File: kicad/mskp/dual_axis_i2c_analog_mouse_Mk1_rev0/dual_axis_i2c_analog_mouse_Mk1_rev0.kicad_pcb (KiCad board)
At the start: 2 copper layers, 17 parts, among them J1 I2C_controller_JST, J2 I2C_controller_pads, J3 mouse_input_pads, J4 mouse_input_JST, J5 Alert_pad, U1 AMS1117-3.3, U2 ADS1115IDGS

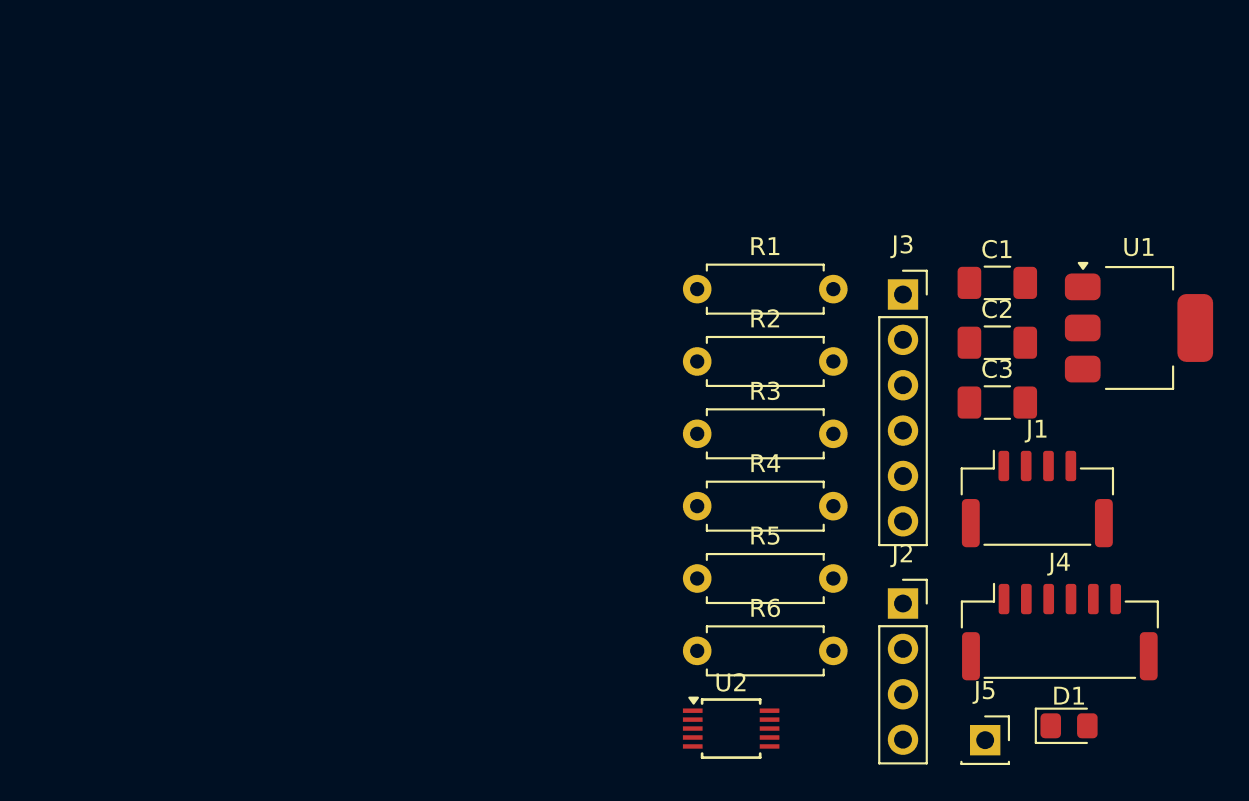
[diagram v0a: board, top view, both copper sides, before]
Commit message: Begins rough PCB part grouping for all control board revisions
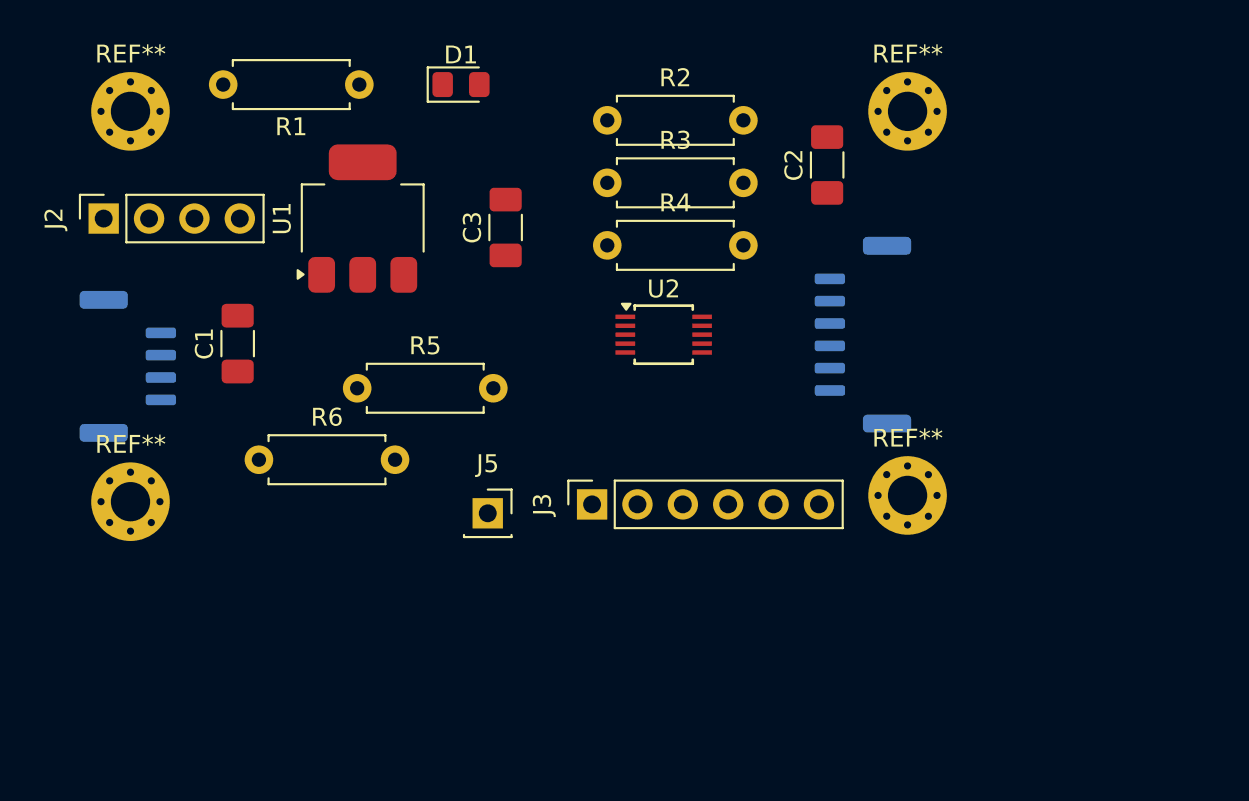
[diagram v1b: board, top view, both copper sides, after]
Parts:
- added REF**: MountingHole_2.2mm_M2_Pad_Via, MountingHole:MountingHole_2.2mm_M2_Pad_Via, F.Cu at (149.5, 69.5)
- added REF**: MountingHole_2.2mm_M2_Pad_Via, MountingHole:MountingHole_2.2mm_M2_Pad_Via, F.Cu at (149.5, 91.0)
- added REF**: MountingHole_2.2mm_M2_Pad_Via, MountingHole:MountingHole_2.2mm_M2_Pad_Via, F.Cu at (106.0, 69.5)
- added REF**: MountingHole_2.2mm_M2_Pad_Via, MountingHole:MountingHole_2.2mm_M2_Pad_Via, F.Cu at (106.0, 91.3)
- J1, J4: moved to B.Cu
- moved J1 51.5 mm to (105.8, 83.8), turned to 90 degrees
- moved J2 49.7 mm to (104.5, 75.5), turned to 90 degrees
- moved D1 49.5 mm to (124.5, 68.0)
- moved U1 43.9 mm to (119.0, 75.5), turned to 90 degrees
- moved C1 42.7 mm to (112.0, 82.5), turned to 90 degrees
- moved J5 30.6 mm to (126.0, 92.0)
- moved C3 29.2 mm to (127.0, 76.0), turned to 90 degrees
- moved R6 26.8 mm to (113.2, 89.0)
- moved U2 22.4 mm to (135.8, 82.0)
- moved R1 22.1 mm to (118.8, 68.0), turned to 180 degrees
- moved R5 21.8 mm to (118.7, 85.0)
- moved J3 21.0 mm to (131.8, 91.5), turned to 90 degrees
- moved J4 20.0 mm to (147.0, 82.0), turned to -90 degrees
- moved R4 15.4 mm to (132.7, 77.0)
- moved R3 14.9 mm to (132.7, 73.5)
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
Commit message: Continues work with rough PCB outlines
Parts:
- moved C2 16.9 mm to (138.4, 88.0), turned to 0 degrees
- moved J3 5.40 mm to (126.4, 91.4)
- moved REF** 5.15 mm to (144.8, 71.6)
- moved REF** 4.94 mm to (144.6, 90.4)
- moved R6 4.72 mm to (114.2, 84.4), turned to -90 degrees
- moved REF** 4.02 mm to (109.8, 70.8)
- moved J5 3.85 mm to (122.2, 91.4)
- moved R1 3.67 mm to (122.0, 69.8)
- moved U2 3.50 mm to (132.4, 82.6)
- moved C1 3.18 mm to (114.2, 80.2)
- moved REF** 2.51 mm to (108.4, 90.6)
- moved U1 2.48 mm to (120.6, 77.4)
- moved D1 2.33 mm to (126.2, 69.6), turned to 180 degrees
- moved C3 2.25 mm to (126.8, 78.2)
- moved J1 2.18 mm to (107.8, 82.8)
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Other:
- board outline added: 43.6 x 26.4 mm

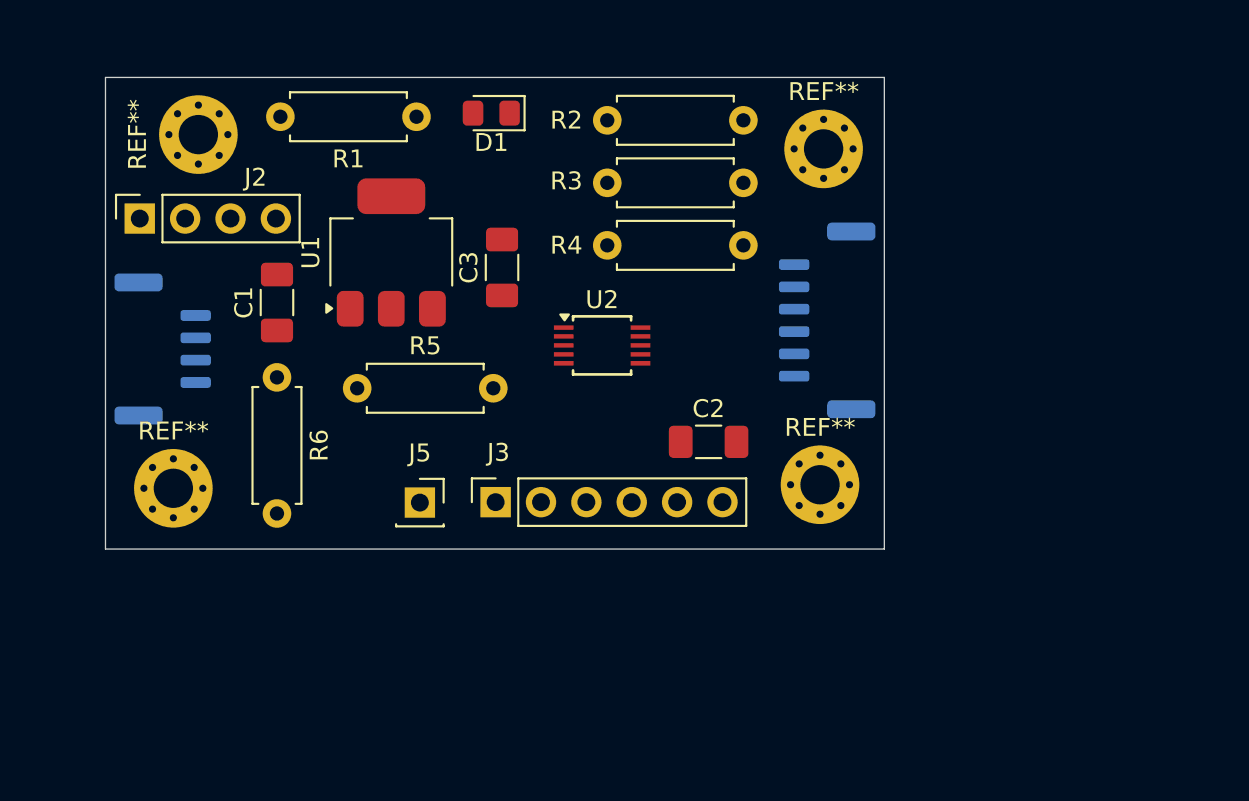
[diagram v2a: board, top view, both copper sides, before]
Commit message: Refines usb and mouse control boards with outline and GND
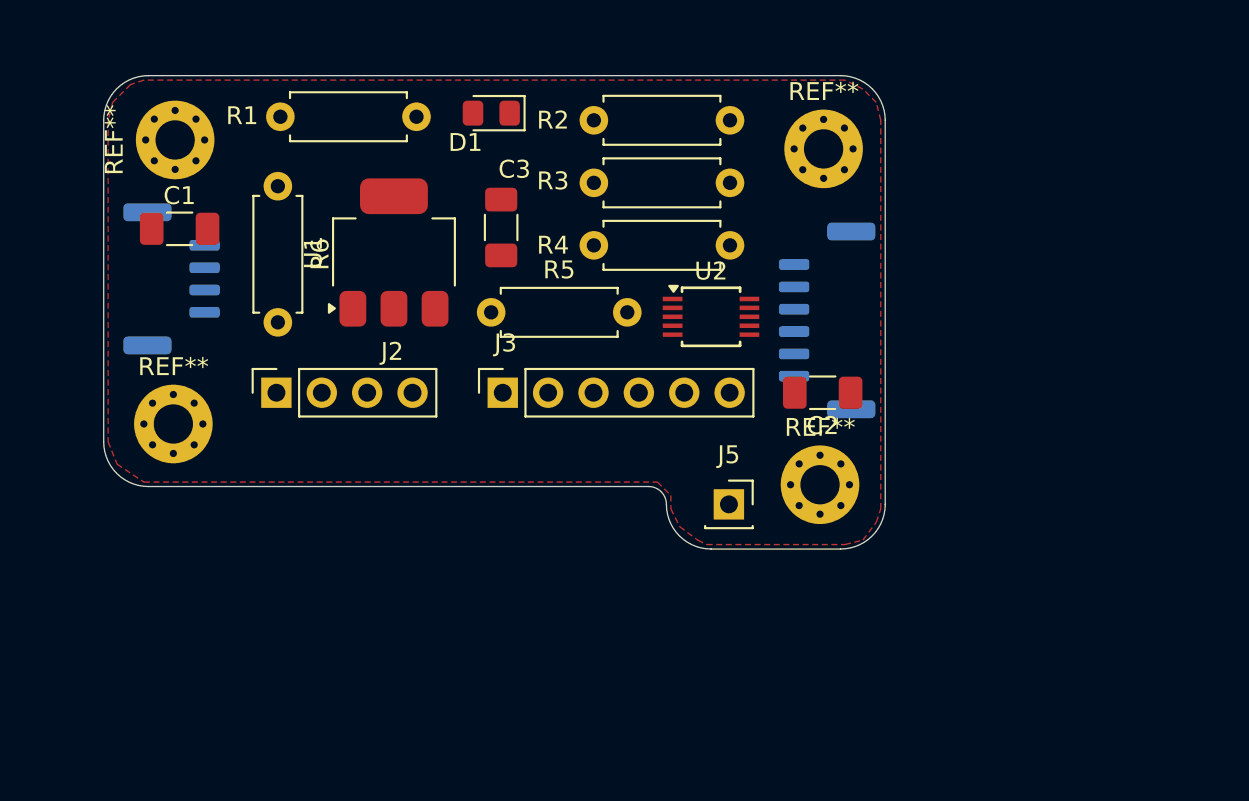
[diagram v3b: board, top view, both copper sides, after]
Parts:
- moved J5 17.3 mm to (139.5, 91.5)
- moved J2 12.4 mm to (114.2, 85.2)
- moved R6 10.7 mm to (114.2, 73.7)
- moved R5 8.62 mm to (126.2, 80.8)
- moved C2 6.95 mm to (144.8, 85.2), turned to 180 degrees
- moved C1 6.84 mm to (108.8, 76.1), turned to 0 degrees
- moved U2 6.31 mm to (138.5, 81.0)
- moved J3 6.14 mm to (126.8, 85.2)
- moved J1 3.96 mm to (108.3, 78.9)
- moved REF** 3.60 mm to (108.4, 87.0)
- moved C3 2.24 mm to (126.8, 76.0)
- moved REF** 1.33 mm to (108.5, 71.1)
- moved R2 0.75 mm to (131.9, 70.0)
- moved R3 0.75 mm to (131.9, 73.5)
- moved R4 0.75 mm to (131.9, 77.0)
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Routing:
- added copper zone on F.Cu, net GND
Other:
- board size 43.6 x 26.4 mm -> 43.8 x 26.5 mm

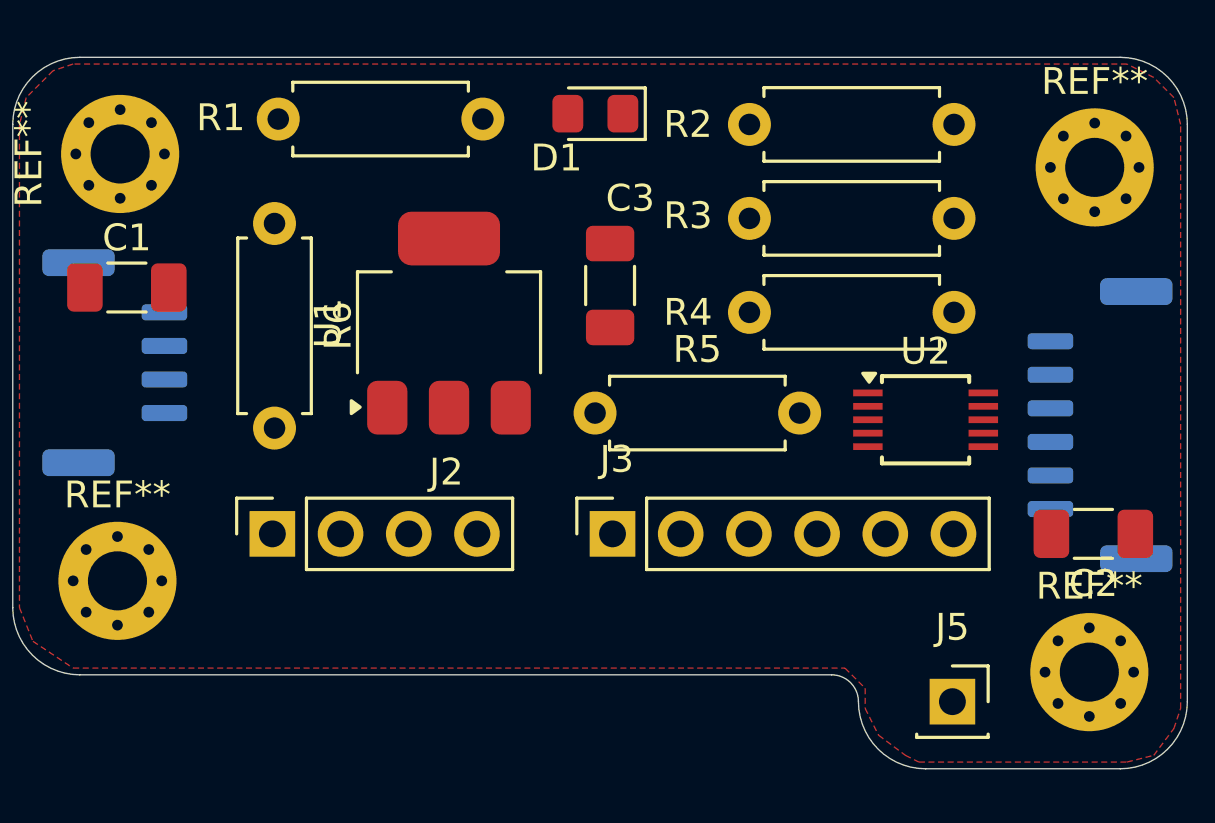
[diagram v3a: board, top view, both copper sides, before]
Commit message: Initial layout of dual_axis_i2c_analog_mouse_Mk1_rev0 PCB traces
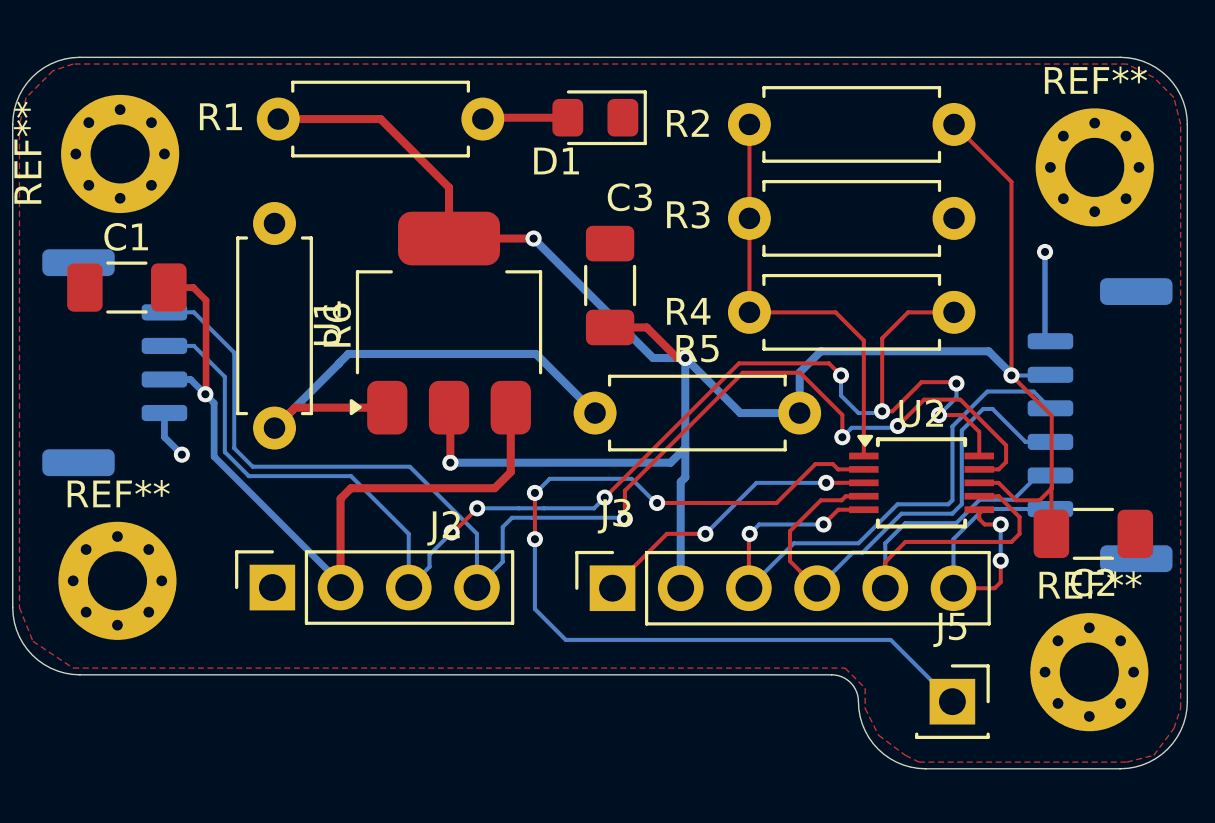
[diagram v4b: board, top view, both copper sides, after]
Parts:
- moved U2 2.35 mm to (138.3, 83.3)
- moved J3 2.03 mm to (126.8, 87.3)
- moved J2 2.00 mm to (114.2, 87.2)
- moved D1 0.15 mm to (126.2, 69.8)
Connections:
- J3 pad 1: Net-(J3-Pin_1) -> GND
- J4 pad 1: Net-(J3-Pin_1) -> GND
- R4 pad 1: Net-(J1-Pin_3) -> /only one resistor needed
- R4 pad 2: /only one resistor needed -> Net-(J1-Pin_3)
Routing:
- net Net-(J3-Pin_2): track 0.00 -> 79.6 mm, vias 0 -> 4
- net Net-(J1-Pin_3): track 0.00 -> 51.4 mm, vias 0 -> 7
- net Net-(J1-Pin_4): track 0.00 -> 48.1 mm, vias 0 -> 3
- net Net-(J5-Pin_1): track 0.00 -> 34.8 mm, vias 0 -> 3
- net Net-(J1-Pin_2): track 0.00 -> 28.6 mm, vias 0 -> 1
- net Net-(J3-Pin_3): track 0.00 -> 22.8 mm, vias 0 -> 2
- net Net-(J3-Pin_4): track 0.00 -> 19.4 mm
- net Net-(U1-GND): track 0.00 -> 18.5 mm
- net Net-(J3-Pin_5): track 0.00 -> 17.7 mm
- net GND: track 0.00 -> 16.2 mm, vias 0 -> 4
- net /only one resistor needed: track 0.00 -> 16.0 mm
- net Net-(J3-Pin_6): track 0.00 -> 11.4 mm, vias 0 -> 2
- net Net-(D1-A): track 0.00 -> 3.19 mm

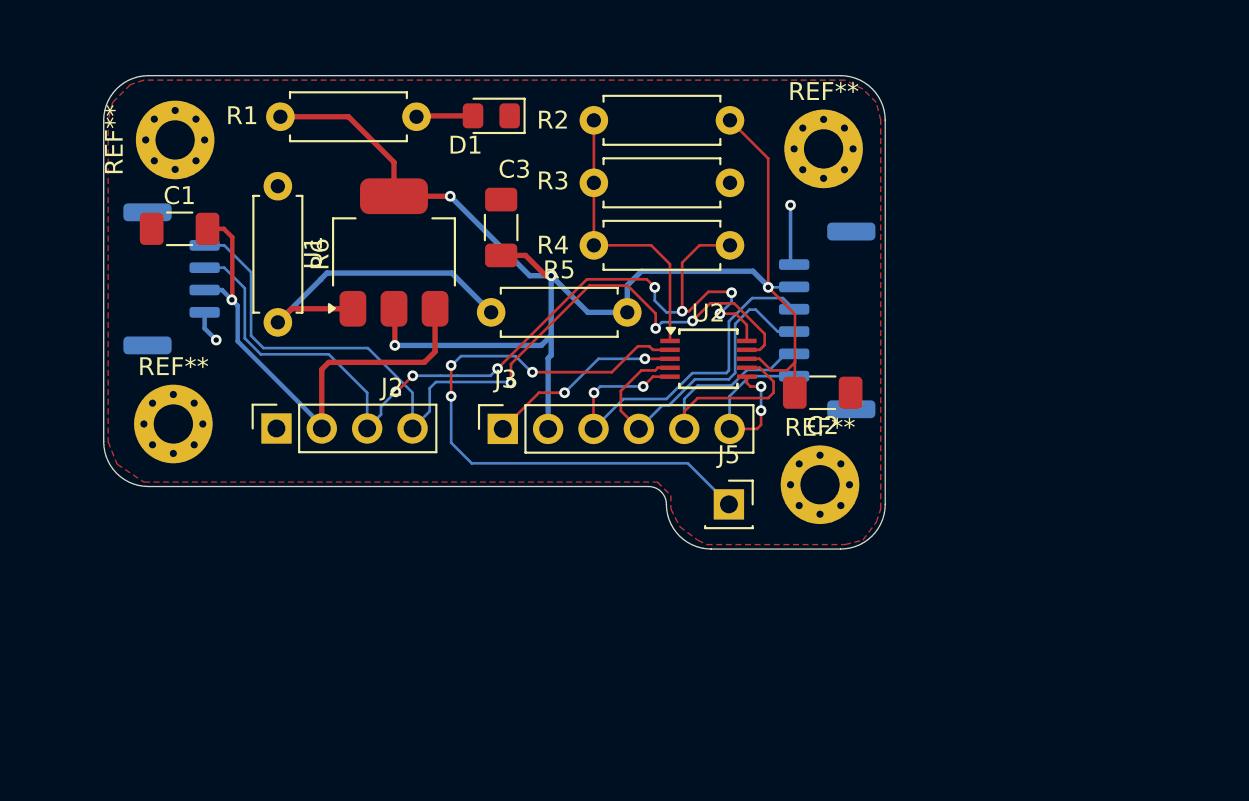
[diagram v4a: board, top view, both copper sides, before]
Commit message: Adds silkscreen for dual_axis_i2c_analog_mouse_Mk1_rev0 PCB
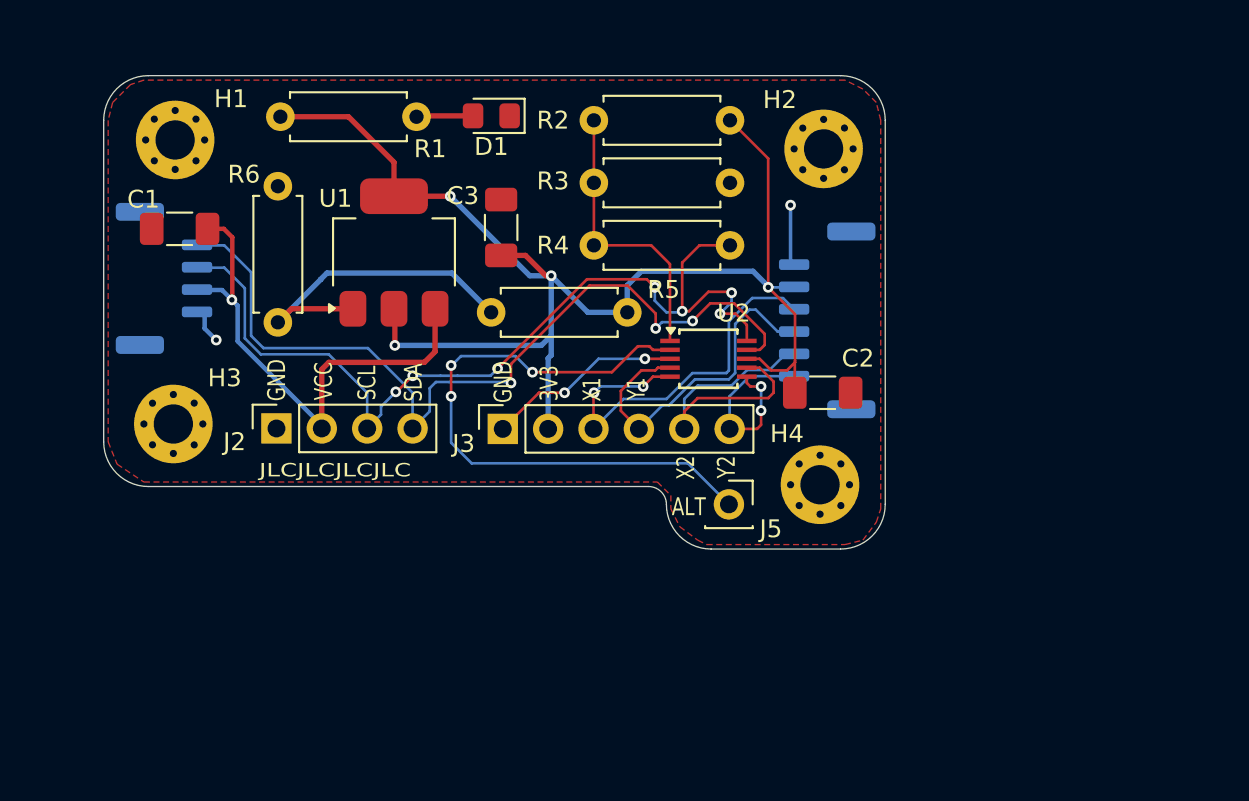
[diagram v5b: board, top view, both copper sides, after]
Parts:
- moved J1 0.43 mm to (107.9, 78.8)
- renumbered REF** to H1, REF** to H2, REF** to H3, REF** to H4
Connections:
- net Net-(J1-Pin_2) renamed /VCC
- net Net-(J1-Pin_3) renamed /SCL
- net Net-(J1-Pin_4) renamed /SDA
- net Net-(J3-Pin_2) renamed /3V3
- net Net-(J3-Pin_3) renamed /X1
- net Net-(J3-Pin_4) renamed /Y1
- net Net-(J3-Pin_5) renamed /X2
- net Net-(J3-Pin_6) renamed /Y2
- net Net-(J5-Pin_1) renamed /ALRT
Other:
- board text added: "10-2024"
- board text added: "3V3"
- board text added: "ALT"
- board text added: "ANALOG IN"
- board text added: "Dual Axis I2C Mouse"
- board text added: "GND"
- board text added: "I"
- board text added: "I2C"
- board text added: "JLCJLCJLCJLC"
- board text added: "MSKP-2AXIS-MOUSE-MK.1-REV.0"
- board text added: "Mk"
- board text added: "SCL"
- board text added: "SDA"
- board text added: "VCC"
- board text added: "X1"
- board text added: "X2"
- board text added: "Y1"
- board text added: "Y2"
- board text added: "github.com/thegreatgramblinham"

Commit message: Final tweaks to PCBs before second round of mskp fabrications
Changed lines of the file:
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@@
 			(plot_on_all_layers_selection 0x0000000_00000000)
 			(disableapertmacros no)
-			(usegerberextensions no)
-			(usegerberattributes yes)
-			(usegerberadvancedattributes yes)
-			(creategerberjobfile yes)
+			(usegerberextensions yes)
+			(usegerberattributes no)
+			(usegerberadvancedattributes no)
+			(creategerberjobfile no)
 			(dashed_line_dash_ratio 12.000000)
 			(dashed_line_gap_ratio 3.000000)
 			(svgprecision 4)
 			(plotframeref no)
-			(viasonmask no)
+			(viasonmask yes)
 			(mode 1)
 			(useauxorigin no)
@@
 			(psa4output no)
 			(plotreference yes)
-			(plotvalue yes)
+			(plotvalue no)
 			(plotfptext yes)
 			(plotinvisibletext no)
 			(sketchpadsonfab no)
-			(subtractmaskfromsilk no)
+			(subtractmaskfromsilk yes)
 			(outputformat 1)
 			(mirror no)
-			(drillshape 1)
+			(drillshape 0)
 			(scaleselection 1)
-			(outputdirectory "")
+			(outputdirectory "i2c_mouse_mk1_exports")
 		)
 	)
@@
 	)
 	(gr_text "JLCJLCJLCJLC"
-		(at 113.2 90.025 0)
+		(at 118.8 89.7 0)
 		(layer "F.SilkS")
 		(effects
